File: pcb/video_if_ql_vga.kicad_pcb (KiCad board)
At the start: 2 copper layers, 31.1 x 66.2 mm, 16 parts, among them J1 Conn_01x05, J2 DB15_Female_HighDensity, U1 SC0915

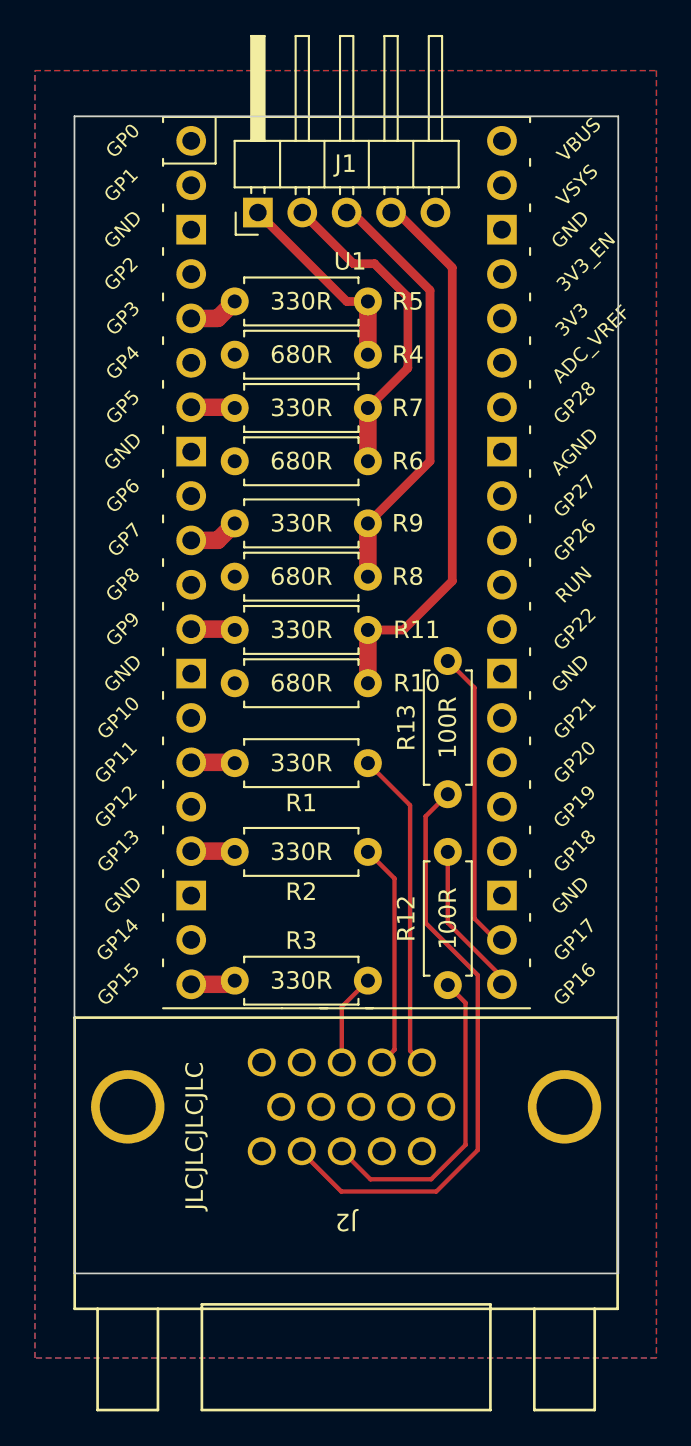
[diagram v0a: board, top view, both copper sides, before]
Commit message: Provide THT combined with SMD footprints for resistors
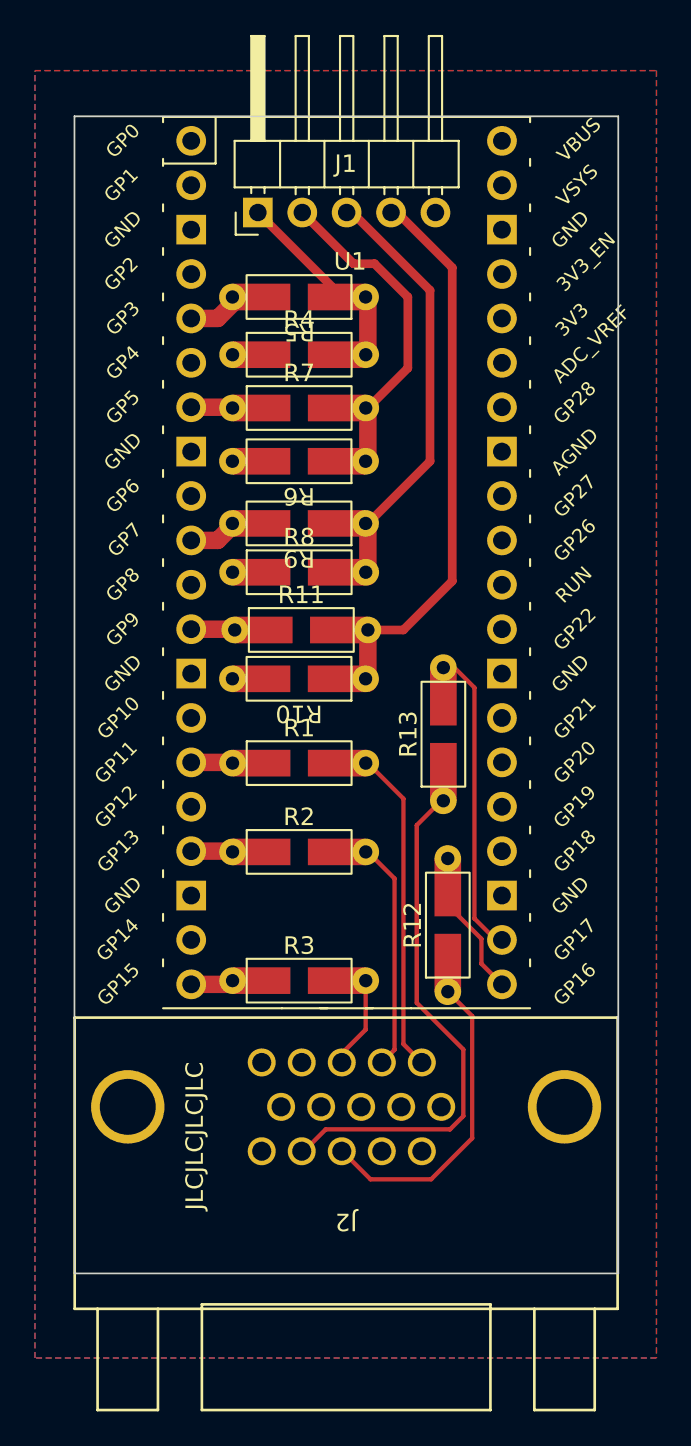
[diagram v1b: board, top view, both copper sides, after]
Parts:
- R1, R10, R11, R12, R13, R2, R3, R4, R5, R6, R7, R8, R9: footprint Resistor_THT:R_Axial_DIN0207_L6.3mm_D2.5mm_P7.62mm_Horizontal -> THT_SMD:R_Axial_DIN0207_L6.3mm_D2.5mm_P7.62_Horizontal
- moved R10 3.95 mm to (139.6, 90.7)
- moved R5 3.95 mm to (139.6, 68.8)
- moved R6 3.94 mm to (139.6, 78.2)
- moved R9 3.94 mm to (139.6, 81.8)
- moved R11 3.81 mm to (139.7, 87.9)
- moved R8 3.70 mm to (139.6, 84.6)
- moved R1 3.69 mm to (139.6, 95.5)
- moved R2 3.69 mm to (139.6, 100.6)
- moved R3 3.69 mm to (139.6, 108.0)
- moved R4 3.69 mm to (139.6, 72.1)
- moved R7 3.69 mm to (139.6, 75.2)
- moved R13 3.44 mm to (147.8, 93.8)
- moved R12 3.43 mm to (148.1, 104.8)
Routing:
- net Net-(J2-Pad14): track 34.2 -> 30.5 mm
